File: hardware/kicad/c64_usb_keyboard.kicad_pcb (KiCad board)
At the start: 2 copper layers, 85 x 55 mm, 35 parts, among them J3 UART DEBUG, U1 Raspberry Pi Pico, U2 74HCT245

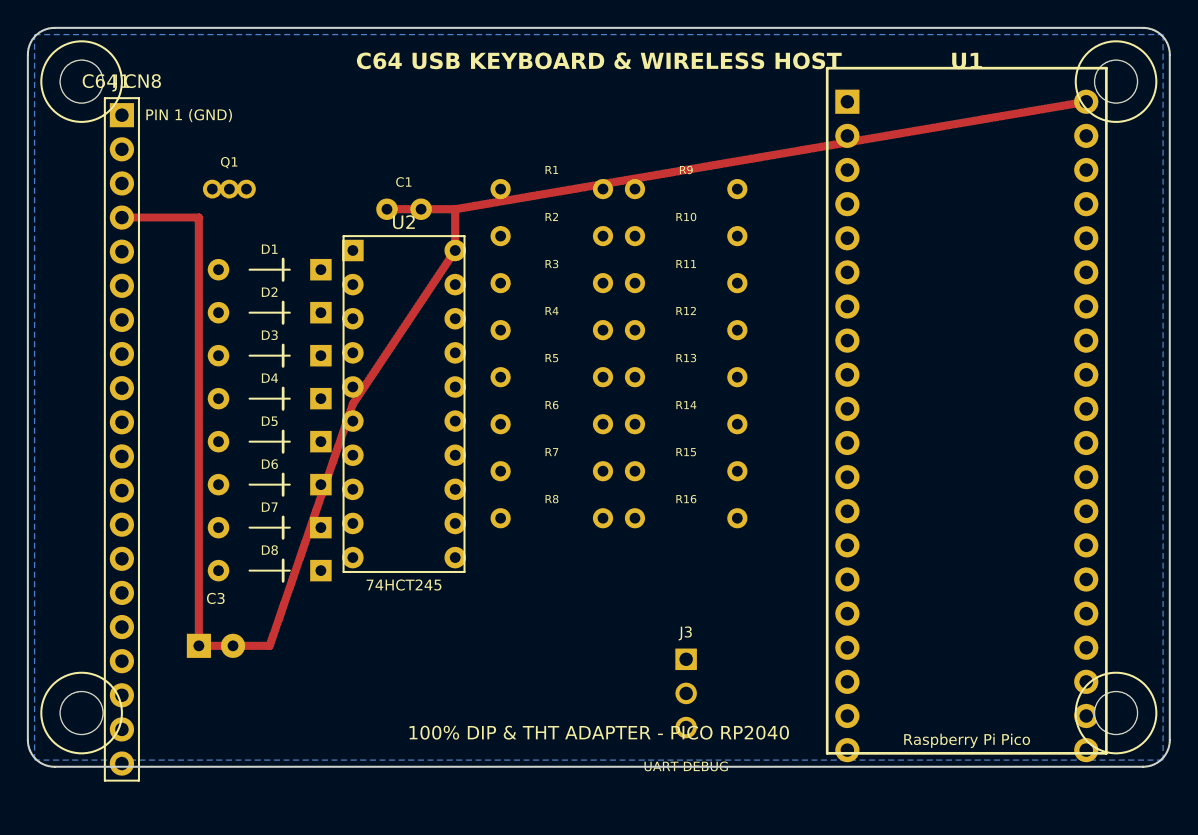
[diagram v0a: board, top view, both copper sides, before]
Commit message: Migrate to Raspberry Pi Pico 2 (RP2350): 5V-tolerant native open-drain matrix, KiCad 8 project fix, and ultra-simplified BOM
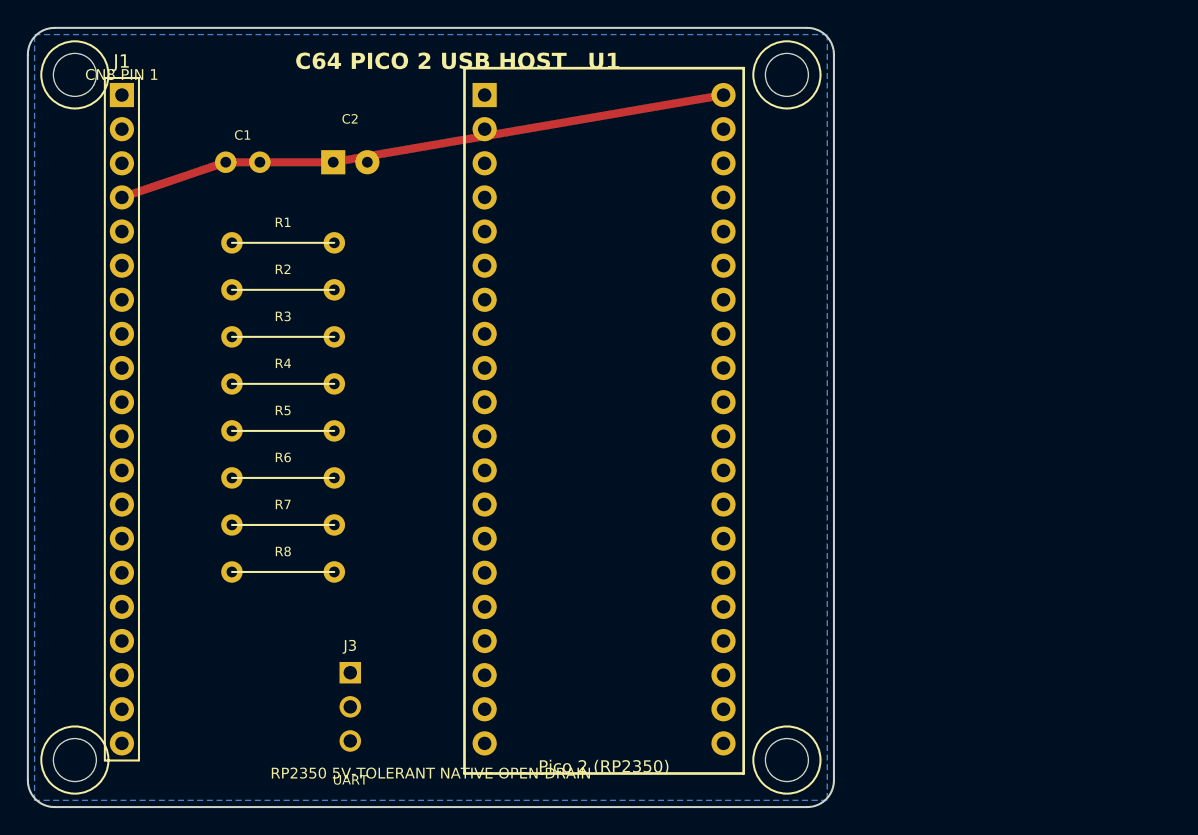
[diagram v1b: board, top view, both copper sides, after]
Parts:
- removed ? (x4): , MountingHole:MountingHole_3.2mm_M3
- removed C3: , Capacitor_THT:CP_Radial_D6.3mm_P2.50mm
- removed D1, D2, D3, D4, D5, D6, D7, D8: , Diode_THT:D_DO-35_SOD27_P7.62mm_Horizontal
- removed Q1: , Package_TO_SOT_THT:TO-92_Inline
- removed R10, R11, R12, R13, R14, R15, R16, R9: , Resistor_THT:R_Axial_DIN0207_L6.3mm_D2.5mm_P7.62mm_Horizontal
- removed U2: 74HCT245, Package_DIP:DIP-20_W7.62mm_Socket
- added C2: 47uF, Capacitor_THT:CP_Radial_D6.3mm_P2.50mm, F.Cu at (24.0, 10.0)
- added H1: , MountingHole:MountingHole_3.2mm_M3, F.Cu at (3.50, 3.50)
- added H2: , MountingHole:MountingHole_3.2mm_M3, F.Cu at (56.5, 3.50)
- added H3: , MountingHole:MountingHole_3.2mm_M3, F.Cu at (3.50, 54.5)
- added H4: , MountingHole:MountingHole_3.2mm_M3, F.Cu at (56.5, 54.5)
- C1: value (none) -> 100nF
- J1: value (none) -> C64_CN8
- J3: value UART DEBUG -> UART
- R1, R2, R3, R4, R5, R6, R7, R8: value (none) -> 100R
- U1: value Raspberry Pi Pico -> Pico 2 (RP2350)
- moved U1 27.0 mm to (34.0, 0.00)
- moved J3 25.0 mm to (24.0, 48.0)
- moved R1 20.4 mm to (19.0, 16.0)
- moved R2 20.4 mm to (19.0, 19.5)
- moved R3 20.4 mm to (19.0, 23.0)
- moved R4 20.4 mm to (19.0, 26.5)
- moved R5 20.4 mm to (19.0, 30.0)
- moved R6 20.4 mm to (19.0, 33.5)
- moved R7 20.4 mm to (19.0, 37.0)
- moved R8 20.4 mm to (19.0, 40.5)
- moved C1 12.5 mm to (16.0, 10.0)
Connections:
- R1 pad 1: C64_COL0 -> C64_ROW0
- R1 pad 2: PICO_COL0 -> PICO_ROW0
- R2 pad 1: C64_COL1 -> C64_ROW1
- R2 pad 2: PICO_COL1 -> PICO_ROW1
- R3 pad 1: C64_COL2 -> C64_ROW2
- R3 pad 2: PICO_COL2 -> PICO_ROW2
- R4 pad 1: C64_COL3 -> C64_ROW3
- R4 pad 2: PICO_COL3 -> PICO_ROW3
- R5 pad 1: C64_COL4 -> C64_ROW4
- R5 pad 2: PICO_COL4 -> PICO_ROW4
- R6 pad 1: C64_COL5 -> C64_ROW5
- R6 pad 2: PICO_COL5 -> PICO_ROW5
- R7 pad 1: C64_COL6 -> C64_ROW6
- R7 pad 2: PICO_COL6 -> PICO_ROW6
- R8 pad 1: C64_COL7 -> C64_ROW7
- R8 pad 2: PICO_COL7 -> PICO_ROW7
- U1 pad 1: PICO_COL0 -> C64_COL0
- U1 pad 10: PICO_COL7 -> C64_COL7
- U1 pad 2: PICO_COL1 -> C64_COL1
- U1 pad 4: PICO_COL2 -> C64_COL2
- U1 pad 5: PICO_COL3 -> C64_COL3
- U1 pad 6: PICO_COL4 -> C64_COL4
- U1 pad 7: PICO_COL5 -> C64_COL5
- U1 pad 9: PICO_COL6 -> C64_COL6
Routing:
- net +5V: track 131.4 -> 45.6 mm
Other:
- board size 85 x 55 mm -> 60 x 58 mm
- board text added: "C64 PICO 2 USB HOST"
- board text added: "CN8 PIN 1"
- board text added: "RP2350 5V-TOLERANT NATIVE OPEN-DRAIN"
- board text removed: "100% DIP & THT ADAPTER - PICO RP2040"
- board text removed: "C64 CN8"
- board text removed: "C64 USB KEYBOARD & WIRELESS HOST"
- board text removed: "PIN 1 (GND)"
